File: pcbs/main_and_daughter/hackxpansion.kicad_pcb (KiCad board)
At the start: 4 copper layers, 52 x 69 mm, 97 parts, among them CN1 533981471, CN2 533981471, CN3 533981471, CN4 533981471, IC1 ADS7128IRTET, J1 Conn_01x03_MountingPin, J2 USB_C_Receptacle_USB2.0_14P, Q1 BSS138, Q2 2N7002, SW1 SW_Push, SW2 SW_Push, SW3 SW_On_Off, U2 RP2354B, U5 SPX3819M5-L-3-3, U7 BQ24075RGT, U8 USBLC6-2SC6, Y1 ABM8-272-T3

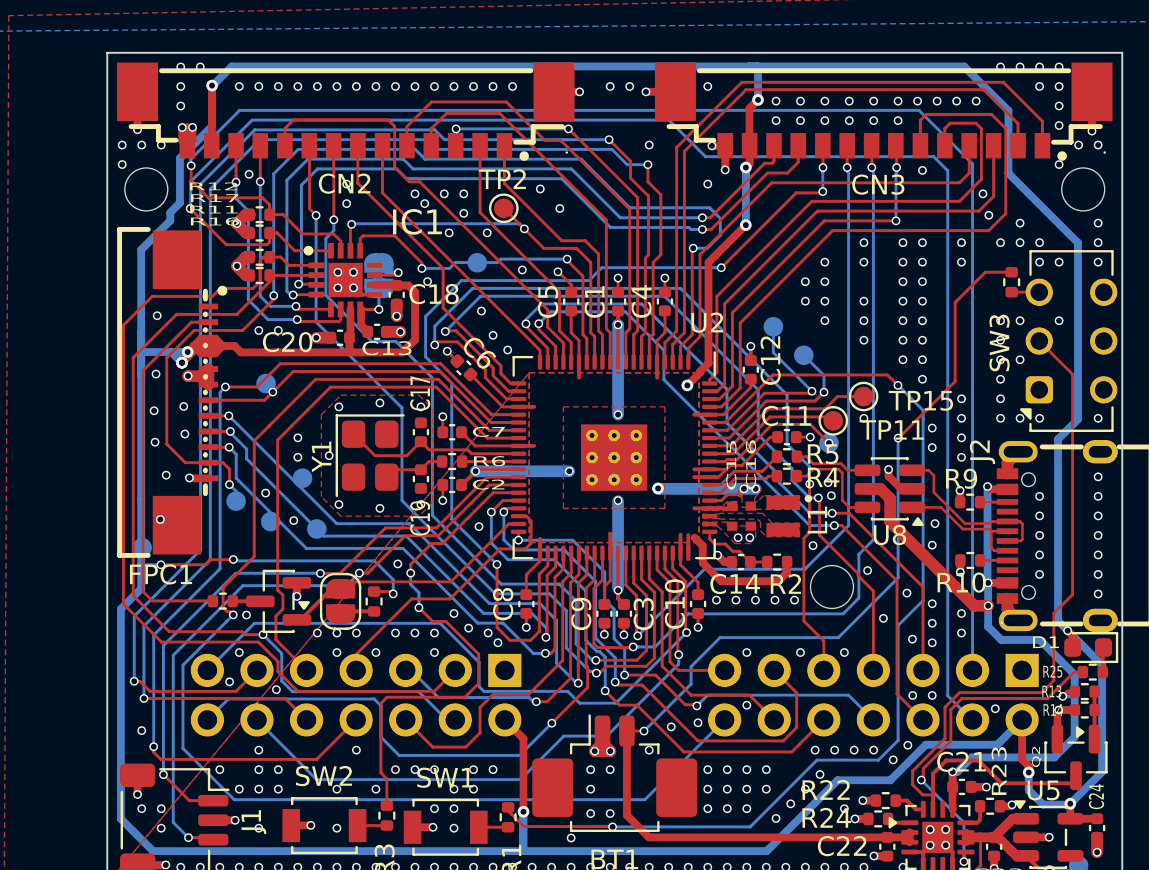
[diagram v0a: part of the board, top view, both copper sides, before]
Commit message: moved fpc connector inwords
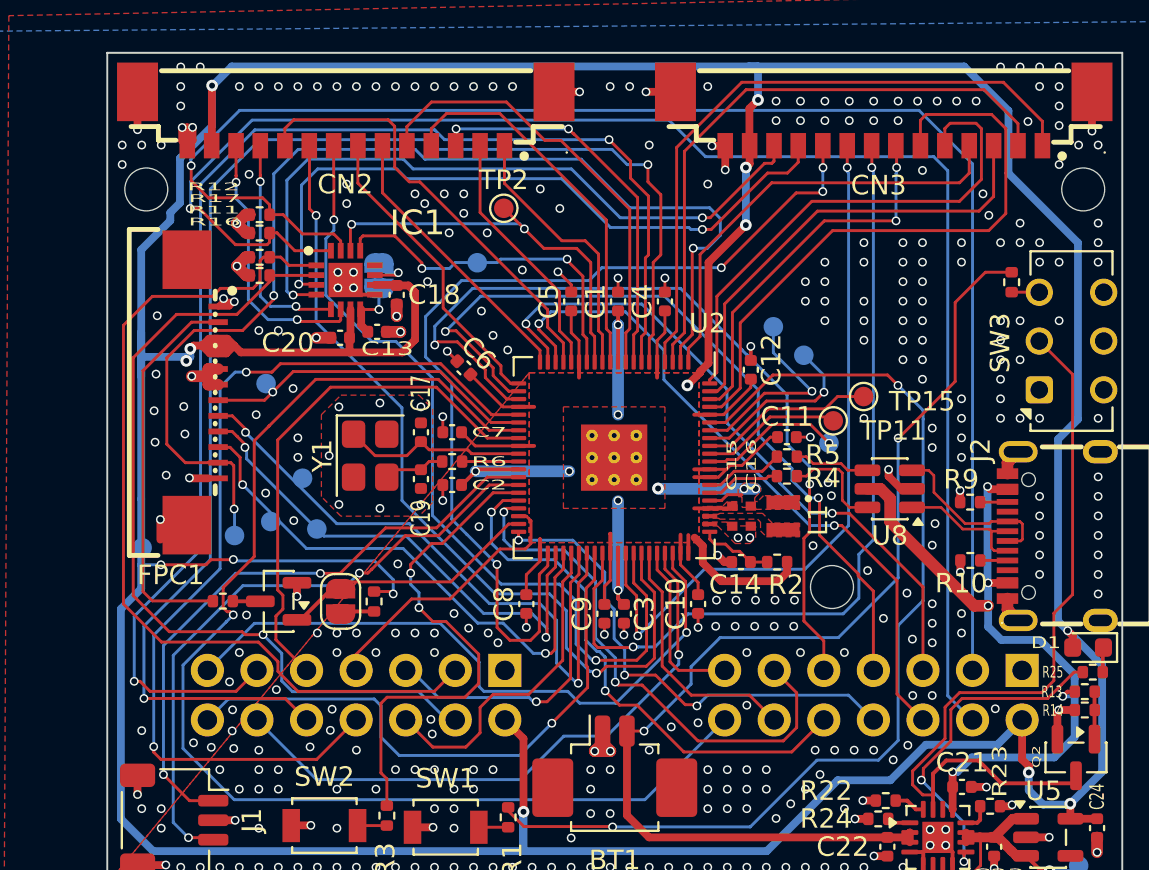
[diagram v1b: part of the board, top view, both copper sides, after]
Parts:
- moved TP8 1.76 mm to (108.4, 82.6)
- moved FPC1 0.50 mm to (106.8, 75.3)
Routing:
- net /GND: track 60.6 -> 63.5 mm, vias 361 -> 381
- net /Main Board/Display/RESET: track 56.6 -> 58.8 mm
- net /+3V3: track 302.7 -> 300.5 mm, vias 15 -> 14
- net /Main Board/Display/DC: track 18.2 -> 17.7 mm

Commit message: started to work on blender
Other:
- board text added: "PCB3D_BR_DAUGHTER"
- board text added: "PCB3D_BR_MAIN"
- board text added: "PCB3D_TL_DAUGHTER"
- board text added: "PCB3D_TL_MAIN"
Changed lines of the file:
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@@
 			(layer "F.SilkS"
 				(type "Top Silk Screen")
+				(color "White")
 			)
 			(layer "F.Paste"
@@
 			(layer "F.Mask"
 				(type "Top Solder Mask")
+				(color "Black")
 				(thickness 0.01)
 			)
@@
 			(layer "B.Mask"
 				(type "Bottom Solder Mask")
+				(color "Black")
 				(thickness 0.01)
 			)
@@
 			(layer "B.SilkS"
 				(type "Bottom Silk Screen")
+				(color "White")
 			)
 			(copper_finish "None")
@@
 		(capping no)
 		(filling no)
+		(zone_defaults)
 		(grid_origin 141.12 43.26)
 		(pcbplotparams
@@
 		(layer "Edge.Cuts")
 	)
+	(gr_text "PCB3D_TL_DAUGHTER"
+		(at 85.27 26.1 0)
+		(layer "Cmts.User")
+		(effects
+			(font
+				(size 1 1)
+				(thickness 0.15)
+			)
+			(justify left bottom)
+		)
+	)
+	(gr_text "PCB3D_TL_MAIN"
+		(at 85.95 56.27 0)
+		(layer "Cmts.User")
+		(effects
+			(font
+				(size 1 1)
+				(thickness 0.15)
+			)
+			(justify left bottom)
+		)
+	)
+	(gr_text "PCB3D_BR_MAIN"
+		(at 165.31 111.46 0)
+		(layer "Cmts.User")
+		(effects
+			(font
+				(size 1 1)
+				(thickness 0.15)
+			)
+			(justify left bottom)
+		)
+	)
+	(gr_text "PCB3D_BR_DAUGHTER"
+		(at 169.45 54.92 0)
+		(layer "Cmts.User")
+		(effects
+			(font
+				(size 1 1)
+				(thickness 0.15)
+			)
+			(justify left bottom)
+		)
+	)
 	(gr_text "{\n  \"ViaStitching\": \"0.2\",\n  \"stitch_zone_0\": {\n    \"HSpacing\": \"1\",\n    \"VSpacing\": \"1\",\n    \"HOffset\": \"0\",\n    \"VOffset\": \"0\",\n    \"Clearance\": \"0\",\n    \"Randomize\": false\n  }\n}"
